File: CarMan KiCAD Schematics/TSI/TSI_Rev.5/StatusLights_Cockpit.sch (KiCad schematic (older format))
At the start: 20 parts, among them Q3 ZVP1320F, U1 RDE03110S12, U11 TLP293, U13 TLP293, U27 TLP293

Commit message: TSI Footprinting (~90%)
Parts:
- C14: footprint (none) -> Capacitor_THT:C_Rect_L18.0mm_W9.0mm_P15.00mm_FKS3_FKP3
- D1: value Power -> Green LED; footprint (none) -> LED_SMD:LED_0805_2012Metric_Pad1.15x1.40mm_HandSolder
- D11: value D_Schottky -> D_Schottky - MMSZ5231B-7-F; footprint (none) -> Diode_SMD:D_SOD-123
- HVPL_LV1: footprint (none) -> TestPoint:TestPoint_Pad_D3.0mm
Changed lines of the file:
@@
 P 10200 1800
 F 0 "D1" V 10300 1900 50  0000 C CNN
-F 1 "Power" H 10200 1926 50  0001 C CNN
-F 2 "" H 10200 1800 50  0001 C CNN
+F 1 "Green LED" H 10200 1926 50  0001 C CNN
+F 2 "LED_SMD:LED_0805_2012Metric_Pad1.15x1.40mm_HandSolder" H 10200 1800 50  0001 C CNN
 F 3 "~" H 10200 1800 50  0001 C CNN
 	1    10200 1800
@@
 F 0 "C14" H 2478 6746 50  0000 L CNN
 F 1 "1u" H 2478 6655 50  0000 L CNN
-F 2 "" H 2300 6700 50  0001 C CNN
-F 3 "~" H 2300 6700 50  0001 C CNN
+F 2 "Capacitor_THT:C_Rect_L18.0mm_W9.0mm_P15.00mm_FKS3_FKP3" H 2300 6700 50  0001 C CNN
+F 3 "https://www.tdk-electronics.tdk.com/inf/20/20/db/fc_2009/B32520_529.pdf" H 2300 6700 50  0001 C CNN
 	1    2300 6700
 	1    0    0    -1
@@
 F 0 "HVPL_LV1" H 4258 6318 50  0000 L CNN
 F 1 "TSAL_LV" H 4258 6227 50  0000 L CNN
-F 2 "" H 4400 6200 50  0001 C CNN
+F 2 "TestPoint:TestPoint_Pad_D3.0mm" H 4400 6200 50  0001 C CNN
 F 3 "~" H 4400 6200 50  0001 C CNN
 	1    4200 6200
@@
 P 6450 1000
 F 0 "D11" V 6300 1100 50  0000 C CNN
-F 1 "D_Schottky" H 6450 1126 50  0001 C CNN
-F 2 "" H 6450 1000 50  0001 C CNN
+F 1 "D_Schottky - MMSZ5231B-7-F" H 6450 1126 50  0001 C CNN
+F 2 "Diode_SMD:D_SOD-123" H 6450 1000 50  0001 C CNN
 F 3 "~" H 6450 1000 50  0001 C CNN
 	1    6450 1000

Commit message: Bug Fixins
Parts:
- removed R25: 300, Resistor_SMD:R_0805_2012Metric_Pad1.15x1.40mm_HandSolder, symbol Device:R
- removed U27: TLP293, Package_SO:SOIC-4_4.55x2.6mm_P1.27mm, symbol TSI_Rev.5-rescue:TLP293-CarMan_KiCAD_Library-TSI_Rev.5-rescue
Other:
- note removed: "Current Ratio 50%"
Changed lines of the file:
@@
-$EndComp
-$Comp
-L TSI_Rev.5-rescue:TLP293-CarMan_KiCAD_Library-TSI_Rev.5-rescue U27
-U 1 1 5F9AA400
-P 4550 2900
-F 0 "U27" H 4550 3100 50  0000 C CNN
-F 1 "TLP293" H 4550 2700 50  0000 C CNN
-F 2 "Package_SO:SOIC-4_4.55x2.6mm_P1.27mm" H 4350 2700 50  0001 L CIN
-F 3 "" H 4550 2900 50  0001 L CNN
-	1    4550 2900
-	1    0    0    -1
 $EndComp
 $Comp
@@
 Text HLabel 1250 1200 0    50   Input ~ 0
 D_LED_CTRL
-Text HLabel 1250 1300 0    50   Input ~ 0
-SPARE_LED_CTRL
+Text HLabel 1250 1500 0    50   Input ~ 0
+24V
+Text HLabel 1250 1800 0    50   Input ~ 0
+GLV_RTN
+Text HLabel 1250 1700 0    50   Input ~ 0
+3.3V
 Text HLabel 1250 1600 0    50   Input ~ 0
-24V
-Text HLabel 1250 1900 0    50   Input ~ 0
-GLV_RTN
-Text HLabel 1250 1800 0    50   Input ~ 0
-3.3V
-Text HLabel 1250 1700 0    50   Input ~ 0
 5V
 Wire Wire Line
@@
 	1250 1200 1400 1200
 Wire Wire Line
-	1250 1300 1400 1300
+	1250 1500 1400 1500
+Wire Wire Line
+	1250 1800 1400 1800
+Wire Wire Line
+	1250 1700 1400 1700
 Wire Wire Line
 	1250 1600 1400 1600
-Wire Wire Line
-	1250 1900 1400 1900
-Wire Wire Line
-	1250 1800 1400 1800
-Wire Wire Line
-	1250 1700 1400 1700
 Text Label 1400 800  0    50   ~ 0
 BP
@@
 Text Label 1400 1200 0    50   ~ 0
 D_LED_CTRL
-Text Label 1400 1300 0    50   ~ 0
-SPARE_LED_CTRL
+Text Label 1400 1500 0    50   ~ 0
+24V
+Text Label 1400 1800 0    50   ~ 0
+GLV_RTN
+Text Label 1400 1700 0    50   ~ 0
+3.3V
 Text Label 1400 1600 0    50   ~ 0
-24V
-Text Label 1400 1900 0    50   ~ 0
-GLV_RTN
-Text Label 1400 1800 0    50   ~ 0
-3.3V
-Text Label 1400 1700 0    50   ~ 0
 5V
 $Comp
@@
 Text Label 5050 1500 0    50   ~ 0
 GLV_RTN
-$Comp
-L Device:R R25
-U 1 1 5F9F8E38
-P 3900 2800
-F 0 "R25" V 3800 2800 50  0000 C CNN
-F 1 "300" V 3900 2800 50  0000 C CNN
-F 2 "Resistor_SMD:R_0805_2012Metric_Pad1.15x1.40mm_HandSolder" V 3830 2800 50  0001 C CNN
-F 3 "~" H 3900 2800 50  0001 C CNN
-	1    3900 2800
-	0    1    1    0
-$EndComp
-Wire Wire Line
-	3750 2800 3500 2800
-Text Label 3750 3000 0    50   ~ 0
-GLV_RTN
-Text Label 5050 3000 0    50   ~ 0
-SPARE_LED
-Text Label 5050 2800 0    50   ~ 0
-24V
-Text Label 3500 2800 2    50   ~ 0
-SPARE_LED_CTRL
 Wire Wire Line
 	7100 600  7100 1100
@@
 Text Notes 7200 1200 0    50   ~ 0
 0.2A Id *CHECK THIS FET, specifications\n are likely not correct.\n Placeholder transistor*
-Text Notes 4200 2550 0    50   ~ 0
-Current Ratio 50%
 $Comp
 L Connector:TestPoint HVPL_LV1
@@
 Wire Notes Line
 	8350 5000 8200 5000
+Text HLabel 1250 1900 0    50   Input ~ 0
+TSAL
+Text HLabel 1250 2100 0    50   Input ~ 0
+TSAL_RTN
+Wire Wire Line
+	1250 1900 1400 1900
+Wire Wire Line
+	1250 2100 1400 2100
+Text Label 1400 1900 0    50   ~ 0
+TSAL
+Text Label 1400 2100 0    50   ~ 0
+TSAL_RTN
 Text HLabel 1250 2000 0    50   Input ~ 0
-TSAL
-Text HLabel 1250 2200 0    50   Input ~ 0
-TSAL_RTN
+TSAL_Cockpit
 Wire Wire Line
 	1250 2000 1400 2000
-Wire Wire Line
-	1250 2200 1400 2200
 Text Label 1400 2000 0    50   ~ 0
-TSAL
-Text Label 1400 2200 0    50   ~ 0
-TSAL_RTN
-Text HLabel 1250 2100 0    50   Input ~ 0
-TSAL_Cockpit
-Wire Wire Line
-	1250 2100 1400 2100
-Text Label 1400 2100 0    50   ~ 0
 TSAL_Cockpit
 Text Label 10200 2350 2    50   ~ 0
@@
 Wire Wire Line
 	10200 1450 10200 1650
-Text HLabel 1250 2400 0    50   Input ~ 0
+Text HLabel 1250 2300 0    50   Input ~ 0
 Drive_BTN_RTN
-Wire Wire Line
-	1250 2400 1400 2400
-Text Label 1400 2400 0    50   ~ 0
-Drive_BTN_RTN
-Text HLabel 1250 2300 0    50   Input ~ 0
-Drive_BTN
 Wire Wire Line
 	1250 2300 1400 2300
 Text Label 1400 2300 0    50   ~ 0
+Drive_BTN_RTN
+Text HLabel 1250 2200 0    50   Input ~ 0
 Drive_BTN
 Wire Wire Line
-	5050 3000 4850 3000
-Wire Wire Line
-	5050 2800 4850 2800
-Wire Wire Line
-	4250 2800 4050 2800
+	1250 2200 1400 2200
+Text Label 1400 2200 0    50   ~ 0
+Drive_BTN
 Wire Wire Line
 	5050 2000 4850 2000
@@
 Wire Wire Line
 	8050 6150 8050 5950
+Text HLabel 1250 1300 0    50   Input ~ 0
+RTDS
+Wire Wire Line
+	1250 1300 1400 1300
+Text Label 1400 1300 0    50   ~ 0
+RTDS
+Text Label 1400 1400 0    50   ~ 0
+RTDS_RTN
 Text HLabel 1250 1400 0    50   Input ~ 0
-RTDS
+RTDS_RTN
 Wire Wire Line
 	1250 1400 1400 1400
-Text Label 1400 1400 0    50   ~ 0
-RTDS
-Text Label 1400 1500 0    50   ~ 0
-RTDS_RTN
-Text HLabel 1250 1500 0    50   Input ~ 0
-RTDS_RTN
-Wire Wire Line
-	1250 1500 1400 1500
 Text Notes 1050 650  0    94   ~ 0
 SIGNALS\n
-Text HLabel 1250 2500 0    50   Input ~ 0
+Text HLabel 1250 2400 0    50   Input ~ 0
 Drive_LED
 Wire Wire Line
-	1250 2500 1400 2500
-Text Label 1400 2500 0    50   ~ 0
+	1250 2400 1400 2400
+Text Label 1400 2400 0    50   ~ 0
 Drive_LED
 Wire Notes Line
@@
 	500  500  500  2600
 Wire Wire Line
-	3750 3000 4250 3000
-Wire Wire Line
 	3750 2200 4250 2200

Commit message: TSI Footprinting (~95%) - Added Silk Screen Images from last years projects (not added to any libraries, just folder)
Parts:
- D11: value D_Schottky - MMSZ5231B-7-F -> MMSZ5231B-7-F
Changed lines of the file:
@@
 Wire Wire Line
 	7100 1950 7100 2150
-$Comp
-L CarMan_KiCAD_Library:D_Schottky D11
-U 1 1 5F9B6857
-P 6450 1000
-F 0 "D11" V 6300 1100 50  0000 C CNN
-F 1 "D_Schottky - MMSZ5231B-7-F" H 6450 1126 50  0001 C CNN
-F 2 "Diode_SMD:D_SOD-123" H 6450 1000 50  0001 C CNN
-F 3 "~" H 6450 1000 50  0001 C CNN
-	1    6450 1000
-	0    1    1    0
-$EndComp
 Text Notes 5000 1650 0    47   ~ 0
 Change \ngate voltage\n
@@
 Wire Wire Line
 	5000 6400 5600 6400
+$Comp
+L CarMan_KiCAD_Library:D_Schottky D11
+U 1 1 5F9B6857
+P 6450 1000
+F 0 "D11" V 6300 1100 50  0000 C CNN
+F 1 "MMSZ5231B-7-F" H 6450 1126 50  0001 C CNN
+F 2 "Diode_SMD:D_SOD-123" H 6450 1000 50  0001 C CNN
+F 3 "~" H 6450 1000 50  0001 C CNN
+	1    6450 1000
+	0    1    1    0
+$EndComp
 $EndSCHEMATC

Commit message: TSI Footprinting (~98%) - Assigned U41 footprint to PS1 footprint. Not able to find PS1 footprint. Referenced last years design and took measurement on PCB. Measured as the same distances between points - Need footprints for K2, K3, K4 & J1
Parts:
- U1: footprint TSI_Rev_2021_Footprint_Lib:DIP1549W45P254L3404H940Q24 -> TSI_Rev_2021_Footprint_Lib:RDE03110S12
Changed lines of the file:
@@
 $Descr A4 11693 8268
 encoding utf-8
-Sheet 4 6
+Sheet 6 6
 Title ""
 Date ""
@@
 F 0 "U1" H 3650 7100 50  0000 C CNN
 F 1 "RDE03110S12" H 3450 6300 50  0000 C CNN
-F 2 "TSI_Rev_2021_Footprint_Lib:DIP1549W45P254L3404H940Q24" H 3250 6850 50  0001 C CNN
+F 2 "TSI_Rev_2021_Footprint_Lib:RDE03110S12" H 3250 6850 50  0001 C CNN
 F 3 "https://www.snapeda.com/parts/RDE03110S12/XP%20Power/datasheet/" H 3250 6850 50  0001 C CNN
 	1    3450 6700

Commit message: TSI (~98.5%)
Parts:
- renumbered HVPL_LV1 to TP12, TSAL_RTN1 to TP14
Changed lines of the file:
@@
 0.2A Id *CHECK THIS FET, specifications\n are likely not correct.\n Placeholder transistor*
 $Comp
-L Connector:TestPoint HVPL_LV1
+L Connector:TestPoint TP12
 U 1 1 5FA80FFC
 P 4200 6200
-F 0 "HVPL_LV1" H 4258 6318 50  0000 L CNN
+F 0 "TP12" H 4258 6318 50  0000 L CNN
 F 1 "TSAL_LV" H 4258 6227 50  0000 L CNN
 F 2 "TestPoint:TestPoint_Pad_D3.0mm" H 4400 6200 50  0001 C CNN
@@
 $EndComp
 $Comp
-L Connector:TestPoint TSAL_RTN1
+L Connector:TestPoint TP14
 U 1 1 5FA8198D
 P 4200 7250
-F 0 "TSAL_RTN1" H 4142 7276 50  0000 R CNN
+F 0 "TP14" H 4142 7276 50  0000 R CNN
 F 1 "TSAL_RTN" H 4142 7367 50  0000 R CNN
 F 2 "TestPoint:TestPoint_Pad_D3.0mm" H 4400 7250 50  0001 C CNN

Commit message: Aesthetics
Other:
- moved on the sheet: C6, D11, Q3, R110, R12, R15, R68, R74, R97, U11, U13

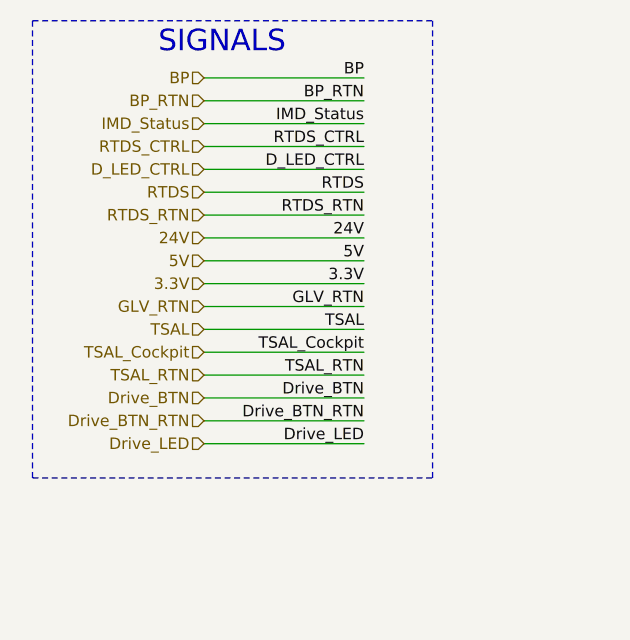
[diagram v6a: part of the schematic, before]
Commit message: TSI Signal Review ISSUES: - PCDC 'Pre_Charge_Ready' and 'PC_Ready' discrepancy - TSI Rev.4 IC1, IC4 -> PCDC & Isolators
REMOVED SIGNALS:
Throttle Plausibility
 - PC_Ready
 - Drive_BTN
 PCDC
 - HV+
 - HV-
 - Throttle_HV
 - IGNI_GND

STATUS LIGHTS & COCKPIT
- BP
- BP_RTN
- IMD_Status
- 5V
- Fault_LED
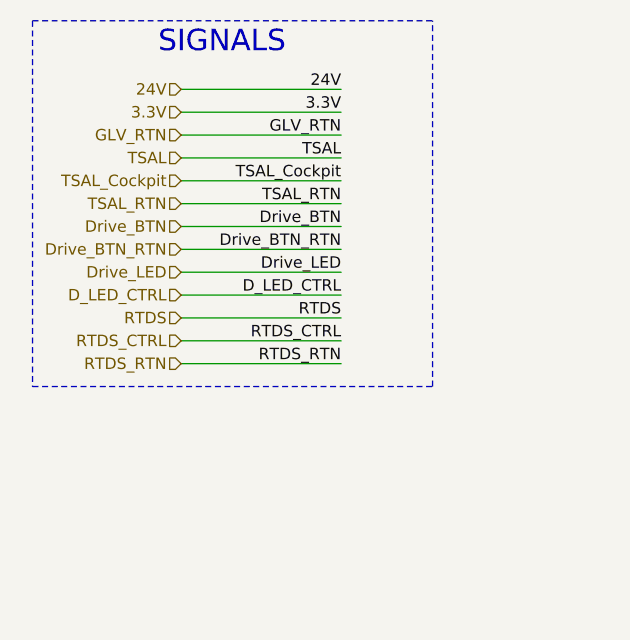
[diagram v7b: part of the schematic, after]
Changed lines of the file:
@@
 $Descr A4 11693 8268
 encoding utf-8
-Sheet 5 6
+Sheet 6 6
 Title ""
 Date ""
@@
 	1    0    0    -1
 $EndComp
-Text HLabel 1250 750  0    50   Input ~ 0
-BP
-Text HLabel 1250 850  0    50   Input ~ 0
-BP_RTN
-Text HLabel 1250 950  0    50   Input ~ 0
-IMD_Status
-Text HLabel 1250 1050 0    50   Input ~ 0
+Text HLabel 1150 1900 0    50   Input ~ 0
 RTDS_CTRL
-Text HLabel 1250 1150 0    50   Input ~ 0
+Text HLabel 1150 1700 0    50   Input ~ 0
 D_LED_CTRL
-Text HLabel 1250 1450 0    50   Input ~ 0
+Text HLabel 1150 800  0    50   Input ~ 0
 24V
-Text HLabel 1250 1750 0    50   Input ~ 0
-GLV_RTN
-Text HLabel 1250 1650 0    50   Input ~ 0
+Text HLabel 1150 1000 0    50   Input ~ 0
+GLV_RTN
+Text HLabel 1150 900  0    50   Input ~ 0
 3.3V
-Text HLabel 1250 1550 0    50   Input ~ 0
-5V
-Text Label 1950 750  2    50   ~ 0
-BP
-Text Label 1950 850  2    50   ~ 0
-BP_RTN
-Text Label 1950 950  2    50   ~ 0
-IMD_Status
-Text Label 1950 1050 2    50   ~ 0
+Text Label 1850 1900 2    50   ~ 0
 RTDS_CTRL
-Text Label 1950 1150 2    50   ~ 0
+Text Label 1850 1700 2    50   ~ 0
 D_LED_CTRL
-Text Label 1950 1450 2    50   ~ 0
+Text Label 1850 800  2    50   ~ 0
 24V
-Text Label 1950 1750 2    50   ~ 0
-GLV_RTN
-Text Label 1950 1650 2    50   ~ 0
+Text Label 1850 1000 2    50   ~ 0
+GLV_RTN
+Text Label 1850 900  2    50   ~ 0
 3.3V
-Text Label 1950 1550 2    50   ~ 0
-5V
 $Comp
 L Device:R R15
@@
 Text Label 10200 5100 0    50   ~ 0
 Drive_BTN_RTN
-Text HLabel 1250 1850 0    50   Input ~ 0
+Text HLabel 1150 1100 0    50   Input ~ 0
 TSAL
-Text HLabel 1250 2050 0    50   Input ~ 0
+Text HLabel 1150 1300 0    50   Input ~ 0
 TSAL_RTN
-Text Label 1950 1850 2    50   ~ 0
+Text Label 1850 1100 2    50   ~ 0
 TSAL
-Text Label 1950 2050 2    50   ~ 0
+Text Label 1850 1300 2    50   ~ 0
 TSAL_RTN
-Text HLabel 1250 1950 0    50   Input ~ 0
+Text HLabel 1150 1200 0    50   Input ~ 0
 TSAL_Cockpit
-Text Label 1950 1950 2    50   ~ 0
+Text Label 1850 1200 2    50   ~ 0
 TSAL_Cockpit
 Text Label 10200 2350 2    50   ~ 0
@@
 Wire Wire Line
 	10200 1450 10200 1650
-Text HLabel 1250 2250 0    50   Input ~ 0
+Text HLabel 1150 1500 0    50   Input ~ 0
 Drive_BTN_RTN
-Text Label 1950 2250 2    50   ~ 0
+Text Label 1850 1500 2    50   ~ 0
 Drive_BTN_RTN
-Text HLabel 1250 2150 0    50   Input ~ 0
+Text HLabel 1150 1400 0    50   Input ~ 0
 Drive_BTN
-Text Label 1950 2150 2    50   ~ 0
+Text Label 1850 1400 2    50   ~ 0
 Drive_BTN
 Wire Wire Line
@@
 Text Notes 7100 6950 0    197  ~ 0
 STATUS LIGHTS & COCKPIT
-Text HLabel 1250 1250 0    50   Input ~ 0
+Text HLabel 1150 1800 0    50   Input ~ 0
 RTDS
-Text Label 1950 1250 2    50   ~ 0
+Text Label 1850 1800 2    50   ~ 0
 RTDS
-Text Label 1950 1350 2    50   ~ 0
+Text Label 1850 2000 2    50   ~ 0
 RTDS_RTN
-Text HLabel 1250 1350 0    50   Input ~ 0
+Text HLabel 1150 2000 0    50   Input ~ 0
 RTDS_RTN
 Text Notes 1050 650  0    94   ~ 0
 SIGNALS\n
-Text HLabel 1250 2350 0    50   Input ~ 0
+Text HLabel 1150 1600 0    50   Input ~ 0
 Drive_LED
-Text Label 1950 2350 2    50   ~ 0
+Text Label 1850 1600 2    50   ~ 0
 Drive_LED
 Wire Notes Line
@@
 $EndComp
 Wire Wire Line
-	1250 2250 1950 2250
-Wire Wire Line
-	1250 2350 1950 2350
-Wire Wire Line
-	1250 2150 1950 2150
-Wire Wire Line
-	1250 750  1950 750
-Wire Wire Line
-	1250 850  1950 850
-Wire Wire Line
-	1250 950  1950 950
-Wire Wire Line
-	1250 1050 1950 1050
-Wire Wire Line
-	1250 1150 1950 1150
-Wire Wire Line
-	1250 1250 1950 1250
-Wire Wire Line
-	1250 1350 1950 1350
-Wire Wire Line
-	1250 1450 1950 1450
-Wire Wire Line
-	1250 1550 1950 1550
-Wire Wire Line
-	1250 1650 1950 1650
-Wire Wire Line
-	1250 1750 1950 1750
-Wire Wire Line
-	1250 1850 1950 1850
-Wire Wire Line
-	1250 1950 1950 1950
-Wire Wire Line
-	1250 2050 1950 2050
-Wire Notes Line
-	2250 500  2250 2500
+	1150 1500 1850 1500
+Wire Wire Line
+	1150 1600 1850 1600
+Wire Wire Line
+	1150 1400 1850 1400
+Wire Wire Line
+	1150 1900 1850 1900
+Wire Wire Line
+	1150 1700 1850 1700
+Wire Wire Line
+	1150 1800 1850 1800
+Wire Wire Line
+	1150 2000 1850 2000
+Wire Wire Line
+	1150 800  1850 800
+Wire Wire Line
+	1150 900  1850 900
+Wire Wire Line
+	1150 1000 1850 1000
+Wire Wire Line
+	1150 1100 1850 1100
+Wire Wire Line
+	1150 1200 1850 1200
+Wire Wire Line
+	1150 1300 1850 1300
 Wire Notes Line
 	500  500  2250 500
-Wire Notes Line
-	500  2500 2250 2500
-Wire Notes Line
-	500  2500 500  500
 Wire Wire Line
 	1100 3900 1750 3900
@@
 Wire Wire Line
 	6200 1750 6750 1750
+Wire Notes Line
+	500  2100 2250 2100
+Wire Notes Line
+	2250 2100 2250 500
+Wire Notes Line
+	500  500  500  2100
 $EndSCHEMATC

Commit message: - Updating TSI
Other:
- note added: "STATUS LIGHTS, TSAL & RTDS"
- note removed: "STATUS LIGHTS & COCKPIT"
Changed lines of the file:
@@
 Wire Wire Line
 	5600 1550 5400 1550
-Text Notes 7100 6950 0    197  ~ 0
-STATUS LIGHTS & COCKPIT
+Text Notes 7100 6950 0    177  ~ 0
+STATUS LIGHTS, TSAL & RTDS
 Text HLabel 1150 1800 0    50   Input ~ 0
 RTDS
